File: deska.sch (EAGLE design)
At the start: 19 parts, among them Q1 BC547, X1 JST-XH-03-PIN-LONG-PAD, X2 JST-XH-03-PIN-LONG-PAD, X3 JST-XH-03-PIN-LONG-PAD, X4 JST-XH-04-PIN-LONG-PAD, X5 JST-XH-04-PIN-LONG-PAD, X6 JST-XH-04-PIN-LONG-PAD

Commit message: deska
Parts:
- added LED2: (no value), led:LED3MM
- added R7: 220, rcl:R-EU_0207/7
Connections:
- removed net N$9: WEMOS1.GND, X4-3.S, X5-3.S, X6-3.S
- new net N$4: LED2.A, R7.2
- net +5V: now also R7.1
- net GND: now also LED2.C, WEMOS1.GND, X4-3.S, X5-3.S, X6-3.S
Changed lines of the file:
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@@
 <grid distance="0.1" unitdist="inch" unit="inch" style="lines" multiple="1" display="no" altdistance="0.01" altunitdist="inch" altunit="inch"/>
 <layers>
-<layer number="1" name="Top" color="4" fill="1" visible="yes" active="no"/>
-<layer number="16" name="Bottom" color="1" fill="1" visible="yes" active="no"/>
-<layer number="17" name="Pads" color="2" fill="1" visible="yes" active="no"/>
-<layer number="18" name="Vias" color="2" fill="1" visible="yes" active="no"/>
-<layer number="19" name="Unrouted" color="6" fill="1" visible="yes" active="no"/>
-<layer number="20" name="Dimension" color="24" fill="1" visible="yes" active="no"/>
-<layer number="21" name="tPlace" color="7" fill="1" visible="yes" active="no"/>
-<layer number="22" name="bPlace" color="7" fill="1" visible="yes" active="no"/>
-<layer number="23" name="tOrigins" color="15" fill="1" visible="yes" active="no"/>
-<layer number="24" name="bOrigins" color="15" fill="1" visible="yes" active="no"/>
-<layer number="25" name="tNames" color="7" fill="1" visible="yes" active="no"/>
-<layer number="26" name="bNames" color="7" fill="1" visible="yes" active="no"/>
-<layer number="27" name="tValues" color="7" fill="1" visible="yes" active="no"/>
-<layer number="28" name="bValues" color="7" fill="1" visible="yes" active="no"/>
+<layer number="1" name="Top" color="4" fill="1" visible="no" active="no"/>
+<layer number="16" name="Bottom" color="1" fill="1" visible="no" active="no"/>
+<layer number="17" name="Pads" color="2" fill="1" visible="no" active="no"/>
+<layer number="18" name="Vias" color="2" fill="1" visible="no" active="no"/>
+<layer number="19" name="Unrouted" color="6" fill="1" visible="no" active="no"/>
+<layer number="20" name="Dimension" color="24" fill="1" visible="no" active="no"/>
+<layer number="21" name="tPlace" color="7" fill="1" visible="no" active="no"/>
+<layer number="22" name="bPlace" color="7" fill="1" visible="no" active="no"/>
+<layer number="23" name="tOrigins" color="15" fill="1" visible="no" active="no"/>
+<layer number="24" name="bOrigins" color="15" fill="1" visible="no" active="no"/>
+<layer number="25" name="tNames" color="7" fill="1" visible="no" active="no"/>
+<layer number="26" name="bNames" color="7" fill="1" visible="no" active="no"/>
+<layer number="27" name="tValues" color="7" fill="1" visible="no" active="no"/>
+<layer number="28" name="bValues" color="7" fill="1" visible="no" active="no"/>
 <layer number="29" name="tStop" color="7" fill="3" visible="no" active="no"/>
 <layer number="30" name="bStop" color="7" fill="6" visible="no" active="no"/>
@@
 <layer number="35" name="tGlue" color="7" fill="4" visible="no" active="no"/>
 <layer number="36" name="bGlue" color="7" fill="5" visible="no" active="no"/>
-<layer number="37" name="tTest" color="7" fill="1" visible="yes" active="no"/>
-<layer number="38" name="bTest" color="7" fill="1" visible="yes" active="no"/>
+<layer number="37" name="tTest" color="7" fill="1" visible="no" active="no"/>
+<layer number="38" name="bTest" color="7" fill="1" visible="no" active="no"/>
 <layer number="39" name="tKeepout" color="4" fill="11" visible="no" active="no"/>
 <layer number="40" name="bKeepout" color="1" fill="11" visible="no" active="no"/>
@@
 <layer number="44" name="Drills" color="7" fill="1" visible="no" active="no"/>
 <layer number="45" name="Holes" color="7" fill="1" visible="no" active="no"/>
-<layer number="46" name="Milling" color="3" fill="1" visible="yes" active="no"/>
-<layer number="47" name="Measures" color="7" fill="1" visible="yes" active="no"/>
-<layer number="48" name="Document" color="7" fill="1" visible="yes" active="no"/>
-<layer number="49" name="Reference" color="7" fill="1" visible="yes" active="no"/>
+<layer number="46" name="Milling" color="3" fill="1" visible="no" active="no"/>
+<layer number="47" name="Measures" color="7" fill="1" visible="no" active="no"/>
+<layer number="48" name="Document" color="7" fill="1" visible="no" active="no"/>
+<layer number="49" name="Reference" color="7" fill="1" visible="no" active="no"/>
 <layer number="50" name="dxf" color="7" fill="1" visible="no" active="no"/>
-<layer number="51" name="tDocu" color="7" fill="1" visible="yes" active="no"/>
-<layer number="52" name="bDocu" color="7" fill="1" visible="yes" active="no"/>
+<layer number="51" name="tDocu" color="7" fill="1" visible="no" active="no"/>
+<layer number="52" name="bDocu" color="7" fill="1" visible="no" active="no"/>
 <layer number="53" name="tGND_GNDA" color="7" fill="9" visible="no" active="no"/>
 <layer number="54" name="bGND_GNDA" color="1" fill="9" visible="no" active="no"/>
@@
 <part name="BUZZER" library="Rembrandt Electronics - JST XH Connectors v1-0" deviceset="JST-XH-02-PIN" device="-LONG-PAD"/>
 <part name="P+2" library="supply1" deviceset="+5V" device=""/>
+<part name="R7" library="rcl" deviceset="R-EU_" device="0207/7" value="220"/>
+<part name="LED2" library="led" library_urn="urn:adsk.eagle:library:259" deviceset="LED" device="3MM" package3d_urn="urn:adsk.eagle:package:15797/1"/>
+<part name="GND2" library="supply1" deviceset="GND" device=""/>
 </parts>
 <sheets>
@@
 <instance part="P+2" gate="1" x="106.68" y="58.42" smashed="yes">
 <attribute name="VALUE" x="104.14" y="53.34" size="1.778" layer="96" rot="R90"/>
+</instance>
+<instance part="R7" gate="G$1" x="73.66" y="96.52" smashed="yes">
+<attribute name="NAME" x="69.85" y="98.0186" size="1.778" layer="95"/>
+<attribute name="VALUE" x="69.85" y="93.218" size="1.778" layer="96"/>
+</instance>
+<instance part="LED2" gate="G$1" x="81.28" y="93.98" smashed="yes">
+<attribute name="NAME" x="84.836" y="89.408" size="1.778" layer="95" rot="R90"/>
+<attribute name="VALUE" x="86.995" y="89.408" size="1.778" layer="96" rot="R90"/>
+</instance>
+<instance part="GND2" gate="1" x="104.14" y="68.58" smashed="yes">
+<attribute name="VALUE" x="101.6" y="66.04" size="1.778" layer="96"/>
 </instance>
 </instances>
@@
 <pinref part="NAPAJENI" gate="-2" pin="KL"/>
 <pinref part="GND6" gate="1" pin="GND"/>
+<wire x1="68.58" y1="91.44" x2="78.74" y2="91.44" width="0.1524" layer="91"/>
+<wire x1="78.74" y1="91.44" x2="78.74" y2="88.9" width="0.1524" layer="91"/>
+<junction x="68.58" y="91.44"/>
+<pinref part="LED2" gate="G$1" pin="C"/>
+<wire x1="78.74" y1="88.9" x2="81.28" y2="88.9" width="0.1524" layer="91"/>
 </segment>
 <segment>
@@
 <wire x1="-27.94" y1="60.96" x2="-27.94" y2="55.88" width="0.1524" layer="91"/>
 <pinref part="RELAY" gate="-3" pin="S"/>
+</segment>
+<segment>
+<pinref part="WEMOS1" gate="D1" pin="GND"/>
+<pinref part="X6" gate="-3" pin="S"/>
+<wire x1="149.86" y1="71.12" x2="149.86" y2="78.74" width="0.1524" layer="91"/>
+<pinref part="X5" gate="-3" pin="S"/>
+<wire x1="132.08" y1="71.12" x2="132.08" y2="78.74" width="0.1524" layer="91"/>
+<wire x1="132.08" y1="71.12" x2="149.86" y2="71.12" width="0.1524" layer="91"/>
+<junction x="132.08" y="71.12"/>
+<wire x1="114.3" y1="71.12" x2="132.08" y2="71.12" width="0.1524" layer="91"/>
+<junction x="114.3" y="71.12"/>
+<pinref part="X4" gate="-3" pin="S"/>
+<wire x1="114.3" y1="78.74" x2="114.3" y2="71.12" width="0.1524" layer="91"/>
+<wire x1="114.3" y1="71.12" x2="104.14" y2="71.12" width="0.1524" layer="91"/>
+<wire x1="104.14" y1="71.12" x2="96.52" y2="71.12" width="0.1524" layer="91"/>
+<wire x1="96.52" y1="71.12" x2="96.52" y2="55.88" width="0.1524" layer="91"/>
+<wire x1="96.52" y1="55.88" x2="81.28" y2="55.88" width="0.1524" layer="91"/>
+<pinref part="GND2" gate="1" pin="GND"/>
+<junction x="104.14" y="71.12"/>
 </segment>
 </net>
@@
 <pinref part="NAPAJENI" gate="-1" pin="KL"/>
 <pinref part="P+5" gate="1" pin="+5V"/>
+<pinref part="R7" gate="G$1" pin="1"/>
+<junction x="68.58" y="96.52"/>
+<pinref part="R7" gate="G$1" pin="1"/>
 </segment>
 <segment>
@@
 </segment>
 </net>
-<net name="N$9" class="0">
-<segment>
-<pinref part="WEMOS1" gate="D1" pin="GND"/>
-<pinref part="X6" gate="-3" pin="S"/>
-<wire x1="149.86" y1="71.12" x2="149.86" y2="78.74" width="0.1524" layer="91"/>
-<pinref part="X5" gate="-3" pin="S"/>
-<wire x1="132.08" y1="71.12" x2="132.08" y2="78.74" width="0.1524" layer="91"/>
-<wire x1="132.08" y1="71.12" x2="149.86" y2="71.12" width="0.1524" layer="91"/>
-<junction x="132.08" y="71.12"/>
-<wire x1="114.3" y1="71.12" x2="132.08" y2="71.12" width="0.1524" layer="91"/>
-<junction x="114.3" y="71.12"/>
-<pinref part="X4" gate="-3" pin="S"/>
-<wire x1="114.3" y1="78.74" x2="114.3" y2="71.12" width="0.1524" layer="91"/>
-<wire x1="114.3" y1="71.12" x2="96.52" y2="71.12" width="0.1524" layer="91"/>
-<wire x1="96.52" y1="71.12" x2="96.52" y2="55.88" width="0.1524" layer="91"/>
-<wire x1="96.52" y1="55.88" x2="81.28" y2="55.88" width="0.1524" layer="91"/>
+<net name="N$4" class="0">
+<segment>
+<pinref part="R7" gate="G$1" pin="2"/>
+<pinref part="LED2" gate="G$1" pin="A"/>
+<wire x1="81.28" y1="96.52" x2="78.74" y2="96.52" width="0.1524" layer="91"/>
 </segment>
 </net>
@@
 will not be understood (or retained) with this version.
 </note>
+<note version="8.3" severity="warning">
+Since Version 8.3, EAGLE supports the association of 3D packages
+with devices in libraries, schematics, and board files. Those 3D
+packages will not be understood (or retained) with this version.
+</note>
 </compatibility>

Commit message: 0.93
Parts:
- added X7: JST-XH-03-PIN-LONG-PAD, Rembrandt Electronics - JST XH Connectors v1-0:JST-XH-03-PIN-LONG-PAD
- LED2: value (none) -> LED2
- NAPAJENI: value (none) -> 5V
- WEMOS1: value (none) -> WEMOS
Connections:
- removed net N$5: R4.1, WEMOS1.D8
- new net N$9: R3.1, WEMOS1.D7, X3-1.S
- net +3V3: now also X7-2.S
- net BUILTINLED: now also R4.1
- net GND: now also X7-1.S
- net N$1: now also WEMOS1.D5; no longer WEMOS1.D0
- net N$19: now also WEMOS1.D6; no longer WEMOS1.D5
- net N$3: now also WEMOS1.D8, X7-3.S; no longer R3.1, WEMOS1.D6, X3-1.S
- net N$8: now also WEMOS1.D0; no longer WEMOS1.D7
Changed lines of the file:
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@@
 <part name="GND4" library="supply1" deviceset="GND" device=""/>
 <part name="GND5" library="supply1" deviceset="GND" device=""/>
-<part name="NAPAJENI" library="con-wago-508" deviceset="W237-02P" device=""/>
+<part name="NAPAJENI" library="con-wago-508" deviceset="W237-02P" device="" value="5V"/>
 <part name="P+5" library="supply1" deviceset="+5V" device=""/>
 <part name="GND6" library="supply1" deviceset="GND" device=""/>
-<part name="WEMOS1" library="wemos" deviceset="WEMOS-D1-MINI" device=""/>
+<part name="WEMOS1" library="wemos" deviceset="WEMOS-D1-MINI" device="" value="WEMOS"/>
 <part name="R5" library="rcl" deviceset="R-EU_" device="0207/7" value="220"/>
 <part name="+3V1" library="supply1" library_urn="urn:adsk.eagle:library:371" deviceset="+3V3" device=""/>
@@
 <part name="P+2" library="supply1" deviceset="+5V" device=""/>
 <part name="R7" library="rcl" deviceset="R-EU_" device="0207/7" value="220"/>
-<part name="LED2" library="led" library_urn="urn:adsk.eagle:library:259" deviceset="LED" device="3MM" package3d_urn="urn:adsk.eagle:package:15797/1"/>
+<part name="LED2" library="led" library_urn="urn:adsk.eagle:library:259" deviceset="LED" device="3MM" package3d_urn="urn:adsk.eagle:package:15797/1" value="LED2"/>
 <part name="GND2" library="supply1" deviceset="GND" device=""/>
+<part name="+3V5" library="supply1" library_urn="urn:adsk.eagle:library:371" deviceset="+3V3" device=""/>
+<part name="X7" library="Rembrandt Electronics - JST XH Connectors v1-0" deviceset="JST-XH-03-PIN" device="-LONG-PAD"/>
+<part name="GND3" library="supply1" deviceset="GND" device=""/>
 </parts>
 <sheets>
@@
 <attribute name="VALUE" x="101.6" y="66.04" size="1.778" layer="96"/>
 </instance>
+<instance part="+3V5" gate="G$1" x="43.18" y="25.4" smashed="yes">
+<attribute name="VALUE" x="40.64" y="20.32" size="1.778" layer="96" rot="R90"/>
+</instance>
+<instance part="X7" gate="-1" x="45.72" y="15.24" smashed="yes" rot="R270">
+<attribute name="NAME" x="44.958" y="12.7" size="1.524" layer="95" rot="R270"/>
+<attribute name="VALUE" x="47.117" y="16.002" size="1.778" layer="96" rot="R270"/>
+</instance>
+<instance part="X7" gate="-2" x="43.18" y="15.24" smashed="yes" rot="R270">
+<attribute name="NAME" x="42.418" y="12.7" size="1.524" layer="95" rot="R270"/>
+</instance>
+<instance part="X7" gate="-3" x="40.64" y="15.24" smashed="yes" rot="R270">
+<attribute name="NAME" x="39.878" y="12.7" size="1.524" layer="95" rot="R270"/>
+</instance>
+<instance part="GND3" gate="1" x="53.34" y="15.24" smashed="yes">
+<attribute name="VALUE" x="50.8" y="12.7" size="1.778" layer="96"/>
+</instance>
 </instances>
 <busses>
@@
 <wire x1="20.32" y1="63.5" x2="20.32" y2="60.96" width="0.1524" layer="91"/>
 <junction x="20.32" y="60.96"/>
-<pinref part="WEMOS1" gate="D1" pin="D0"/>
-<wire x1="48.26" y1="66.04" x2="33.02" y2="66.04" width="0.1524" layer="91"/>
-<wire x1="33.02" y1="66.04" x2="33.02" y2="60.96" width="0.1524" layer="91"/>
 <wire x1="-2.54" y1="88.9" x2="12.7" y2="88.9" width="0.1524" layer="91"/>
 <pinref part="X1" gate="-1" pin="S"/>
-</segment>
-</net>
-<net name="N$3" class="0">
-<segment>
-<wire x1="38.1" y1="53.34" x2="15.24" y2="53.34" width="0.1524" layer="91"/>
-<wire x1="15.24" y1="53.34" x2="7.62" y2="53.34" width="0.1524" layer="91"/>
-<pinref part="R3" gate="G$1" pin="1"/>
-<wire x1="7.62" y1="58.42" x2="7.62" y2="53.34" width="0.1524" layer="91"/>
-<wire x1="15.24" y1="63.5" x2="15.24" y2="53.34" width="0.1524" layer="91"/>
-<junction x="15.24" y="53.34"/>
-<pinref part="WEMOS1" gate="D1" pin="D6"/>
-<wire x1="48.26" y1="60.96" x2="38.1" y2="60.96" width="0.1524" layer="91"/>
-<wire x1="38.1" y1="60.96" x2="38.1" y2="53.34" width="0.1524" layer="91"/>
-<wire x1="-2.54" y1="58.42" x2="7.62" y2="58.42" width="0.1524" layer="91"/>
-<pinref part="X3" gate="-1" pin="S"/>
+<pinref part="WEMOS1" gate="D1" pin="D5"/>
+<wire x1="48.26" y1="63.5" x2="33.02" y2="63.5" width="0.1524" layer="91"/>
+<wire x1="33.02" y1="63.5" x2="33.02" y2="60.96" width="0.1524" layer="91"/>
 </segment>
 </net>
@@
 <junction x="104.14" y="71.12"/>
 </segment>
-</net>
-<net name="N$5" class="0">
-<segment>
-<wire x1="27.94" y1="45.72" x2="27.94" y2="38.1" width="0.1524" layer="91"/>
-<wire x1="27.94" y1="38.1" x2="25.4" y2="38.1" width="0.1524" layer="91"/>
-<pinref part="R4" gate="G$1" pin="1"/>
-<pinref part="WEMOS1" gate="D1" pin="D8"/>
-<wire x1="48.26" y1="55.88" x2="43.18" y2="55.88" width="0.1524" layer="91"/>
-<wire x1="43.18" y1="55.88" x2="43.18" y2="45.72" width="0.1524" layer="91"/>
-<wire x1="43.18" y1="45.72" x2="27.94" y2="45.72" width="0.1524" layer="91"/>
+<segment>
+<pinref part="X7" gate="-1" pin="S"/>
+<pinref part="GND3" gate="1" pin="GND"/>
+<wire x1="45.72" y1="17.78" x2="53.34" y2="17.78" width="0.1524" layer="91"/>
 </segment>
 </net>
@@
 <pinref part="R7" gate="G$1" pin="1"/>
 <junction x="68.58" y="96.52"/>
-<pinref part="R7" gate="G$1" pin="1"/>
 </segment>
 <segment>
@@
 <junction x="17.78" y="55.88"/>
 <wire x1="17.78" y1="55.88" x2="10.16" y2="55.88" width="0.1524" layer="91"/>
-<pinref part="WEMOS1" gate="D1" pin="D5"/>
 <wire x1="10.16" y1="73.66" x2="10.16" y2="55.88" width="0.1524" layer="91"/>
-<wire x1="48.26" y1="63.5" x2="35.56" y2="63.5" width="0.1524" layer="91"/>
-<wire x1="35.56" y1="63.5" x2="35.56" y2="55.88" width="0.1524" layer="91"/>
 <wire x1="-2.54" y1="73.66" x2="10.16" y2="73.66" width="0.1524" layer="91"/>
 <pinref part="X2" gate="-1" pin="S"/>
+<pinref part="WEMOS1" gate="D1" pin="D6"/>
+<wire x1="48.26" y1="60.96" x2="35.56" y2="60.96" width="0.1524" layer="91"/>
+<wire x1="35.56" y1="60.96" x2="35.56" y2="55.88" width="0.1524" layer="91"/>
 </segment>
 </net>
@@
 </segment>
 </net>
-<net name="N$8" class="0">
-<segment>
-<pinref part="WEMOS1" gate="D1" pin="D7"/>
-<wire x1="48.26" y1="58.42" x2="40.64" y2="58.42" width="0.1524" layer="91"/>
-<wire x1="40.64" y1="58.42" x2="40.64" y2="40.64" width="0.1524" layer="91"/>
-<pinref part="R6" gate="G$1" pin="2"/>
-<wire x1="40.64" y1="40.64" x2="116.84" y2="40.64" width="0.1524" layer="91"/>
-</segment>
-</net>
 <net name="BUILTINLED" class="0">
 <segment>
@@
 <wire x1="81.28" y1="58.42" x2="86.36" y2="58.42" width="0.1524" layer="91"/>
 <label x="86.36" y="58.42" size="1.778" layer="95"/>
+<wire x1="86.36" y1="58.42" x2="86.36" y2="35.56" width="0.1524" layer="91"/>
+<wire x1="27.94" y1="38.1" x2="25.4" y2="38.1" width="0.1524" layer="91"/>
+<pinref part="R4" gate="G$1" pin="1"/>
+<wire x1="86.36" y1="35.56" x2="27.94" y2="35.56" width="0.1524" layer="91"/>
+<wire x1="27.94" y1="35.56" x2="27.94" y2="38.1" width="0.1524" layer="91"/>
 </segment>
 </net>
@@
 <pinref part="X3" gate="-2" pin="S"/>
 </segment>
+<segment>
+<pinref part="+3V5" gate="G$1" pin="+3V3"/>
+<wire x1="43.18" y1="22.86" x2="43.18" y2="17.78" width="0.1524" layer="91"/>
+<pinref part="X7" gate="-2" pin="S"/>
+</segment>
 </net>
 <net name="N$4" class="0">
@@
 </segment>
 </net>
+<net name="N$9" class="0">
+<segment>
+<pinref part="WEMOS1" gate="D1" pin="D7"/>
+<wire x1="48.26" y1="58.42" x2="38.1" y2="58.42" width="0.1524" layer="91"/>
+<wire x1="38.1" y1="53.34" x2="15.24" y2="53.34" width="0.1524" layer="91"/>
+<wire x1="15.24" y1="53.34" x2="7.62" y2="53.34" width="0.1524" layer="91"/>
+<pinref part="R3" gate="G$1" pin="1"/>
+<wire x1="7.62" y1="58.42" x2="7.62" y2="53.34" width="0.1524" layer="91"/>
+<wire x1="15.24" y1="63.5" x2="15.24" y2="53.34" width="0.1524" layer="91"/>
+<junction x="15.24" y="53.34"/>
+<wire x1="-2.54" y1="58.42" x2="7.62" y2="58.42" width="0.1524" layer="91"/>
+<pinref part="X3" gate="-1" pin="S"/>
+<wire x1="38.1" y1="58.42" x2="38.1" y2="53.34" width="0.1524" layer="91"/>
+</segment>
+</net>
+<net name="N$8" class="0">
+<segment>
+<pinref part="WEMOS1" gate="D1" pin="D0"/>
+<wire x1="48.26" y1="66.04" x2="45.72" y2="66.04" width="0.1524" layer="91"/>
+<pinref part="R6" gate="G$1" pin="2"/>
+<wire x1="45.72" y1="66.04" x2="45.72" y2="40.64" width="0.1524" layer="91"/>
+<wire x1="45.72" y1="40.64" x2="116.84" y2="40.64" width="0.1524" layer="91"/>
+</segment>
+</net>
+<net name="N$3" class="0">
+<segment>
+<pinref part="WEMOS1" gate="D1" pin="D8"/>
+<wire x1="48.26" y1="55.88" x2="40.64" y2="55.88" width="0.1524" layer="91"/>
+<wire x1="40.64" y1="17.78" x2="40.64" y2="55.88" width="0.1524" layer="91"/>
+<pinref part="X7" gate="-3" pin="S"/>
+</segment>
+</net>

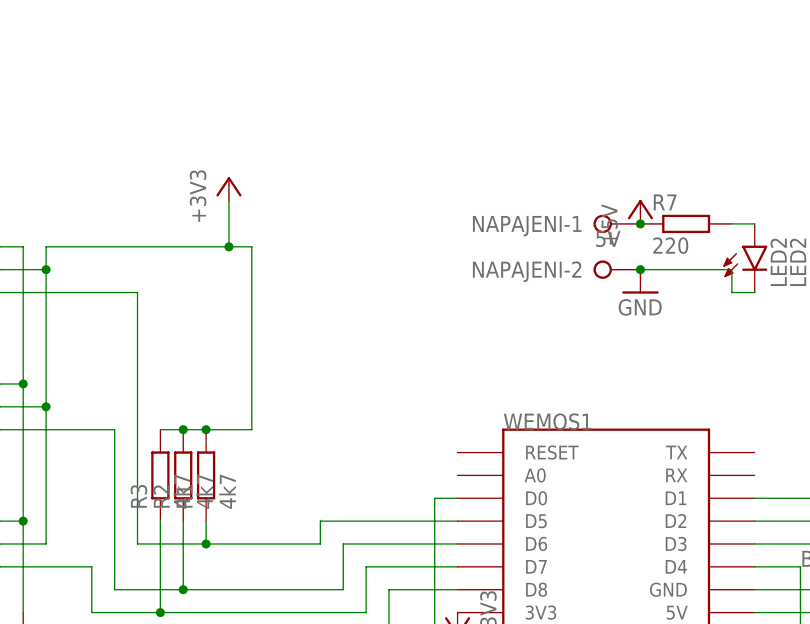
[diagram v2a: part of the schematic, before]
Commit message: +reset pin na desku +popis pinu
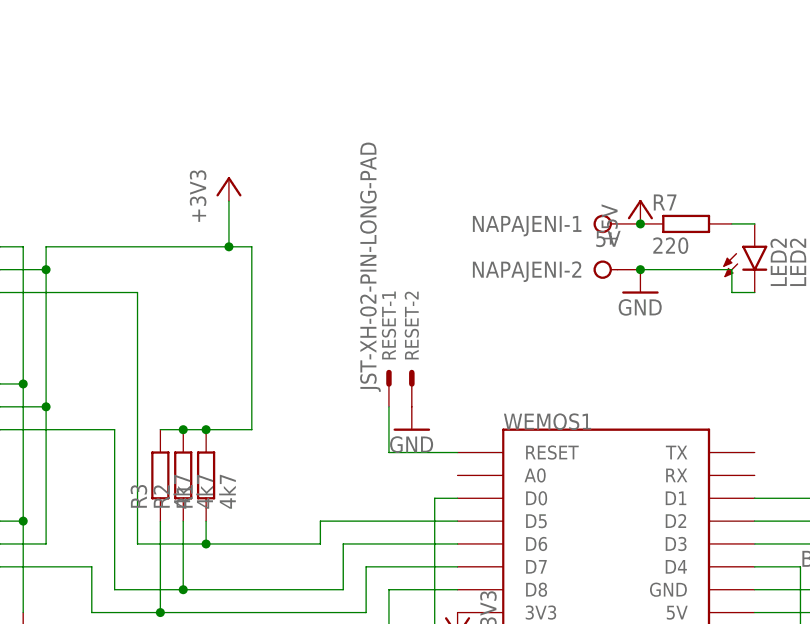
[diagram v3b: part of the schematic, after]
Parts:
- added RESET: JST-XH-02-PIN-LONG-PAD, Rembrandt Electronics - JST XH Connectors v1-0:JST-XH-02-PIN-LONG-PAD
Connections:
- new net N$5: RESET-1.S, WEMOS1.RESET
- net GND: now also RESET-2.S
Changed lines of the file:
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@@
 <part name="X7" library="Rembrandt Electronics - JST XH Connectors v1-0" deviceset="JST-XH-03-PIN" device="-LONG-PAD"/>
 <part name="GND3" library="supply1" deviceset="GND" device=""/>
+<part name="RESET" library="Rembrandt Electronics - JST XH Connectors v1-0" deviceset="JST-XH-02-PIN" device="-LONG-PAD"/>
+<part name="GND7" library="supply1" deviceset="GND" device=""/>
 </parts>
 <sheets>
@@
 <instance part="GND3" gate="1" x="53.34" y="15.24" smashed="yes">
 <attribute name="VALUE" x="50.8" y="12.7" size="1.778" layer="96"/>
+</instance>
+<instance part="RESET" gate="-2" x="43.18" y="78.74" smashed="yes" rot="R90">
+<attribute name="NAME" x="43.942" y="81.28" size="1.524" layer="95" rot="R90"/>
+</instance>
+<instance part="RESET" gate="-1" x="40.64" y="78.74" smashed="yes" rot="R90">
+<attribute name="NAME" x="41.402" y="81.28" size="1.524" layer="95" rot="R90"/>
+<attribute name="VALUE" x="39.243" y="77.978" size="1.778" layer="96" rot="R90"/>
+</instance>
+<instance part="GND7" gate="1" x="43.18" y="73.66" smashed="yes">
+<attribute name="VALUE" x="40.64" y="71.12" size="1.778" layer="96"/>
 </instance>
 </instances>
@@
 <pinref part="GND3" gate="1" pin="GND"/>
 <wire x1="45.72" y1="17.78" x2="53.34" y2="17.78" width="0.1524" layer="91"/>
+</segment>
+<segment>
+<pinref part="RESET" gate="-2" pin="S"/>
+<pinref part="GND7" gate="1" pin="GND"/>
 </segment>
 </net>
@@
 </segment>
 </net>
+<net name="N$5" class="0">
+<segment>
+<pinref part="RESET" gate="-1" pin="S"/>
+<wire x1="40.64" y1="76.2" x2="40.64" y2="71.12" width="0.1524" layer="91"/>
+<pinref part="WEMOS1" gate="D1" pin="RESET"/>
+<wire x1="40.64" y1="71.12" x2="48.26" y2="71.12" width="0.1524" layer="91"/>
+</segment>
+</net>
